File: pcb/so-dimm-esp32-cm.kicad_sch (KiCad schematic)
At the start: 9 parts, among them IC1 PI4IOE5V9535LEX, IC2 PI4IOE5V9535LEX

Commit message: remove components from the BOM which are DNP
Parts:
- TP7, TP8, TP9: now left out of the parts list
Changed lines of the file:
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@@
   )
   (symbol (lib_id "Connector:TestPoint_Small") (at 153.67 111.76 0) (unit 1)
-    (in_bom yes) (on_board yes)
+    (in_bom no) (on_board yes)
     (property "Reference" "TP9" (id 0) (at 149.86 110.49 0)
       (effects (font (size 1.27 1.27)) (justify left))
@@
   )
   (symbol (lib_id "Connector:TestPoint_Small") (at 153.67 104.14 0) (unit 1)
-    (in_bom yes) (on_board yes)
+    (in_bom no) (on_board yes)
     (property "Reference" "TP7" (id 0) (at 149.86 102.87 0)
       (effects (font (size 1.27 1.27)) (justify left))
@@
   )
   (symbol (lib_id "Connector:TestPoint_Small") (at 153.67 107.95 0) (unit 1)
-    (in_bom yes) (on_board yes)
+    (in_bom no) (on_board yes)
     (property "Reference" "TP8" (id 0) (at 149.86 106.68 0)
       (effects (font (size 1.27 1.27)) (justify left))

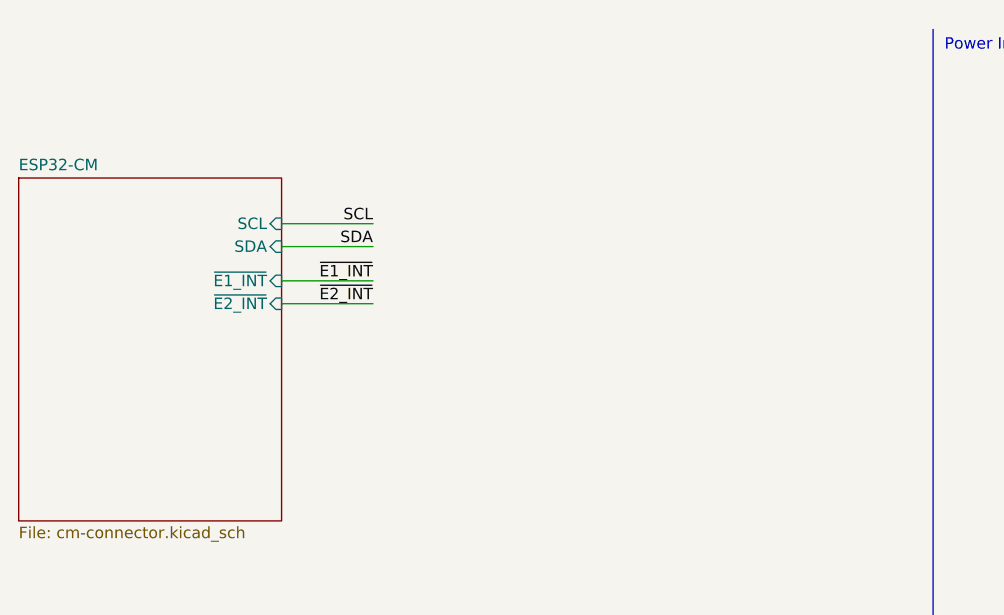
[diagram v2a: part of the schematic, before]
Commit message: Added jumper to swap I2C-0 with I2C-1 for the GPIO-Expanders
The GPIO expanders are using 0x20 and 0x21 as addresses and to avoid clashes with existing carrierboards I made the I2Cchannel switchable. Default is I2C-0 now
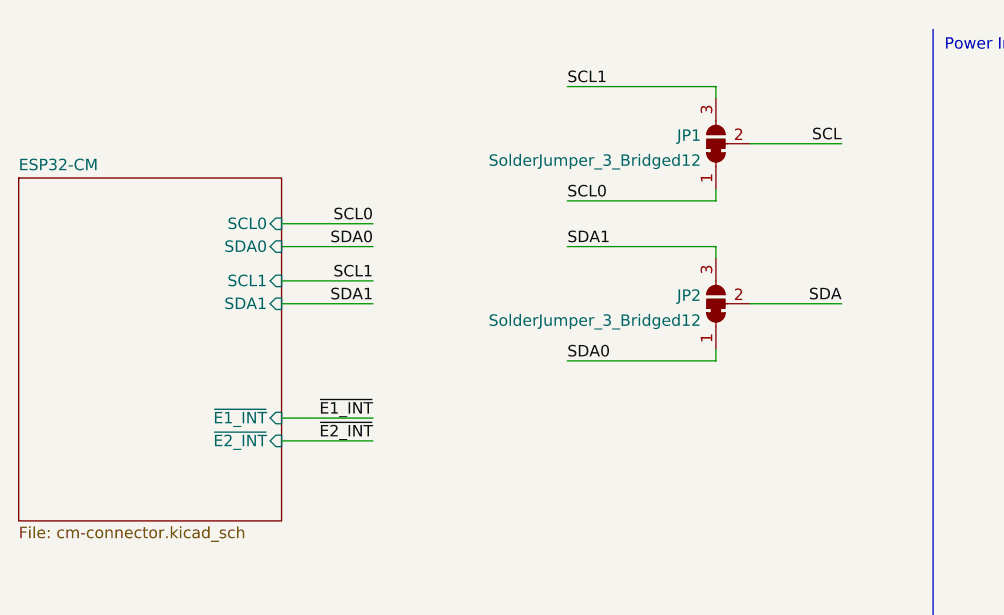
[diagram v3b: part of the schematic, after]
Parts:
- added JP1, JP2: SolderJumper_3_Bridged12, Jumper:SolderJumper-3_P1.3mm_Bridged12_RoundedPad1.0x1.5mm, symbol Jumper:SolderJumper_3_Bridged12
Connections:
- net SCL: now also JP1.2 (C)
- net SDA: now also JP2.2 (C)
- new net SCL0: JP1.1 (A)
- new net SCL1: JP1.3 (B)
- new net SDA0: JP2.1 (A)
- new net SDA1: JP2.3 (B)
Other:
- sheet ESP32-CM ports: added SCL0, SCL1, SDA0, SDA1; removed SCL, SDA
